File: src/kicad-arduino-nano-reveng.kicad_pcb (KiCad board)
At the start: 2 copper layers, 43.8 x 18.4 mm, 14 parts

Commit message: back layer components
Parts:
- removed the REF** at (111.8, 59.1)
- removed the REF** at (111.8, 57.6)
- removed the REF** at (111.8, 56.1)
- added REF**: Crystal_SMD_MicroCrystal_CC7V-T1A-2Pin_3.2x1.5mm, Crystal:Crystal_SMD_MicroCrystal_CC7V-T1A-2Pin_3.2x1.5mm, B.Cu at (85.6, 62.0)
- added REF**: C_0603_1608Metric, Capacitor_SMD:C_0603_1608Metric, B.Cu at (81.8, 61.5)
- added REF**: C_0603_1608Metric, Capacitor_SMD:C_0603_1608Metric, B.Cu at (91.4, 61.5)
- added REF**: C_0603_1608Metric, Capacitor_SMD:C_0603_1608Metric, B.Cu at (96.5, 55.9)
- added REF**: SOT-223, Package_TO_SOT_SMD:SOT-223, B.Cu at (110.7, 59.4)
- added REF**: SOIC-16_3.9x9.9mm_P1.27mm, Package_SO:SOIC-16_3.9x9.9mm_P1.27mm, B.Cu at (88.9, 56.8)
- added REF**: PinHeader_2x03_P2.54mm_Vertical, Connector_PinHeader_2.54mm:PinHeader_2x03_P2.54mm_Vertical, F.Cu at (117.3, 54.3)
- added REF**: C_0603_1608Metric, Capacitor_SMD:C_0603_1608Metric, B.Cu at (110.2, 52.3)
- added REF**: LED_0603_1608Metric_Pad1.05x0.95mm_HandSolder, LED_SMD:LED_0603_1608Metric_Pad1.05x0.95mm_HandSolder, F.Cu at (111.1, 59.3)
- added REF**: LED_0603_1608Metric_Pad1.05x0.95mm_HandSolder, LED_SMD:LED_0603_1608Metric_Pad1.05x0.95mm_HandSolder, F.Cu at (111.1, 57.7)
- added REF**: LED_0603_1608Metric_Pad1.05x0.95mm_HandSolder, LED_SMD:LED_0603_1608Metric_Pad1.05x0.95mm_HandSolder, F.Cu at (111.1, 56.0)
- added REF**: CP_EIA-3216-10_Kemet-I, Capacitor_Tantalum_SMD:CP_EIA-3216-10_Kemet-I, B.Cu at (110.2, 54.4)
- added REF**: CP_EIA-3216-10_Kemet-I, Capacitor_Tantalum_SMD:CP_EIA-3216-10_Kemet-I, B.Cu at (80.0, 52.8)
- added REF**: C_0603_1608Metric, Capacitor_SMD:C_0603_1608Metric, B.Cu at (79.2, 54.6)
- added REF**: D_SOD-123, Diode_SMD:D_SOD-123, B.Cu at (80.8, 56.8)
- added REF**: R_0603_1608Metric, Resistor_SMD:R_0603_1608Metric, B.Cu at (96.5, 57.9)
- added REF**: R_0603_1608Metric, Resistor_SMD:R_0603_1608Metric, B.Cu at (96.5, 59.4)
- added e: R_0603_1608Metric, Resistor_SMD:R_0603_1608Metric, B.Cu at (106.7, 62.5)
- REF** (x4): value R_0603_1608Metric_Pad1.05x0.95mm_HandSolder -> R_0603_1608Metric; footprint Resistor_SMD:R_0603_1608Metric_Pad1.05x0.95mm_HandSolder -> Resistor_SMD:R_0603_1608Metric
- REF**: value USB_Mini-B_Wuerth_65100516121_Horizontal -> USB_Mini-B_Lumberg_2486_01_Horizontal; footprint Connector_USB:USB_Mini-B_Wuerth_65100516121_Horizontal -> Connector_USB:USB_Mini-B_Lumberg_2486_01_Horizontal
- moved REF** 0.68 mm to (111.1, 54.4)
- moved REF** 0.68 mm to (108.0, 59.3)
- moved REF** 0.68 mm to (108.0, 54.4)
- moved REF** 0.64 mm to (108.0, 56.0)
- moved REF** 0.64 mm to (108.0, 57.7)
- moved REF** 0.64 mm to (81.3, 56.8)
- moved REF** 0.63 mm to (99.7, 52.1)
- moved REF** 0.31 mm to (117.2, 48.9)
- moved REF** 0.31 mm to (117.2, 64.8)

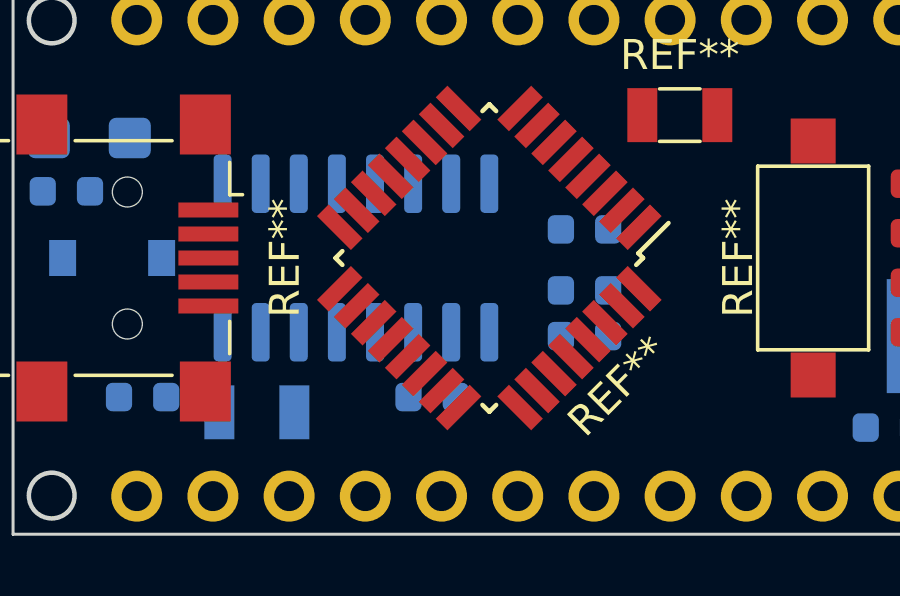
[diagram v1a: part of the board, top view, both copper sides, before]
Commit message: Sch front side components
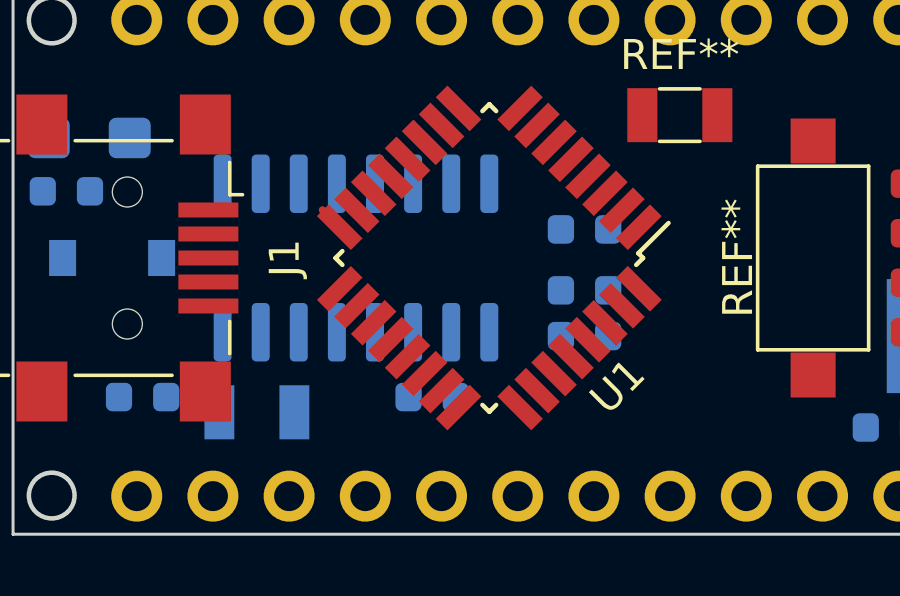
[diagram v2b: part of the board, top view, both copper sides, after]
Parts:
- renumbered REF** to J1, REF** to U1
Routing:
- net (no net): track 0.00 -> 1.71 mm

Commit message: Wiring
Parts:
- removed REF** (x3): LED_0603_1608Metric_Pad1.05x0.95mm_HandSolder, LED_SMD:LED_0603_1608Metric_Pad1.05x0.95mm_HandSolder
- added D2: TX, LED_SMD:LED_0603_1608Metric_Pad1.05x0.95mm_HandSolder, F.Cu at (111.1, 56.0)
- added D3: PWR, LED_SMD:LED_0603_1608Metric_Pad1.05x0.95mm_HandSolder, F.Cu at (111.1, 57.7)
- added D4: L, LED_SMD:LED_0603_1608Metric_Pad1.05x0.95mm_HandSolder, F.Cu at (111.1, 59.3)
- C1, C6: renamed from REF**; value CP_EIA-3216-10_Kemet-I -> CP
- C2, C3, C4, C5, C7: renamed from REF**; value C_0603_1608Metric -> C
- D1: renamed from REF**; value LED_0603_1608Metric_Pad1.05x0.95mm_HandSolder -> RX
- D5: renamed from REF**; value D_SOD-123 -> D_Schottky
- J1: value USB_Mini-B_Lumberg_2486_01_Horizontal -> USB_B_Mini
- J2: renamed from REF**; value PinHeader_2x03_P2.54mm_Vertical -> ISP
- J3, J4: renamed from REF**; value PinHeader_1x15_P2.54mm_Vertical -> Conn_01x15
- R1: renamed from e; value R_0603_1608Metric -> 103
- R2, R3: renamed from REF**; value R_0603_1608Metric -> R
- R4, R5, R6, R7: renamed from REF**; value R_0603_1608Metric -> 102
- SW1: renamed from REF**; value SW_SPST_CK_RS282G05A3 -> RESET
- U1: renamed from REF**; value SOT-223 -> AMS1117-5.0
- U2: renamed from U1; value TQFP-32_7x7mm_P0.8mm -> ATmega328P-AU
- U3: renamed from REF**; value SOIC-16_3.9x9.9mm_P1.27mm -> CH340G
- Y1: renamed from REF**; value Crystal_SMD_3215-2Pin_3.2x1.5mm -> Crystal_Atmega
- Y2: renamed from REF**; value Crystal_SMD_MicroCrystal_CC7V-T1A-2Pin_3.2x1.5mm -> Crystal
- moved J2 5.65 mm to (119.9, 59.4), turned to 180 degrees
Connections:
- C1 pad 1: (no net) -> +5V
- C1 pad 2: (no net) -> GND
- C2 pad 1: (no net) -> +5V
- C2 pad 2: (no net) -> GND
- C3 pad 1: (no net) -> RST
- C3 pad 2: (no net) -> DTR
- C4 pad 1: (no net) -> GND
- C4 pad 2: (no net) -> AREF
- C5 pad 1: (no net) -> GND
- C5 pad 2: (no net) -> 3V3
- C6 pad 1: (no net) -> VUSB
- C6 pad 2: (no net) -> GND
- C7 pad 1: (no net) -> VUSB
- C7 pad 2: (no net) -> GND
- D1 pad 1: (no net) -> RX0
- D1 pad 2: (no net) -> Net-(D1-Pad2)
- D5 pad 1: (no net) -> +5V
- D5 pad 2: (no net) -> VUSB
- J1 pad 1: (no net) -> VUSB
- J1 pad 2: (no net) -> D-
- J1 pad 3: (no net) -> D+
- J1 pad 4: (no net) -> Net-(J1-Pad4)
- J1 pad 5: (no net) -> GND
- J1 pad 6: (no net) -> GND
- J2 pad 1: (no net) -> D12
- J2 pad 2: (no net) -> +5V
- J2 pad 3: (no net) -> D13
- J2 pad 4: (no net) -> D11
- J2 pad 5: (no net) -> RST
- J2 pad 6: (no net) -> GND
- J3 pad 1: (no net) -> TX1
- J3 pad 10: (no net) -> D7
- J3 pad 11: (no net) -> D8
- J3 pad 12: (no net) -> D9
- J3 pad 13: (no net) -> D10
- J3 pad 14: (no net) -> D11
- J3 pad 15: (no net) -> D12
- J3 pad 2: (no net) -> RX0
- J3 pad 3: (no net) -> RST
- J3 pad 4: (no net) -> GND
- J3 pad 5: (no net) -> D2
- J3 pad 6: (no net) -> D3
- J3 pad 7: (no net) -> D4
- J3 pad 8: (no net) -> D5
- J3 pad 9: (no net) -> D6
- J4 pad 1: (no net) -> VIN
- J4 pad 10: (no net) -> A2
- J4 pad 11: (no net) -> A1
- J4 pad 12: (no net) -> A0
- J4 pad 13: (no net) -> AREF
- J4 pad 14: (no net) -> 3V3
- J4 pad 15: (no net) -> D13
- J4 pad 2: (no net) -> GND
- J4 pad 3: (no net) -> RST
- J4 pad 4: (no net) -> +5V
- J4 pad 5: (no net) -> A7
- J4 pad 6: (no net) -> A6
- J4 pad 7: (no net) -> A5
- J4 pad 8: (no net) -> A4
- J4 pad 9: (no net) -> A3
- R1 pad 1: (no net) -> +5V
- R1 pad 2: (no net) -> RST
- R2 pad 1: (no net) -> RXD
- R2 pad 2: (no net) -> TX1
- R3 pad 1: (no net) -> TXD
- R3 pad 2: (no net) -> RX0
- R4 pad 1: (no net) -> Net-(D1-Pad2)
- R4 pad 2: (no net) -> +5V
- R5 pad 1: (no net) -> Net-(D2-Pad2)
- R5 pad 2: (no net) -> +5V
- R6 pad 1: (no net) -> Net-(D3-Pad2)
- R6 pad 2: (no net) -> +5V
- R7 pad 1: (no net) -> Net-(D4-Pad2)
- R7 pad 2: (no net) -> D13
- SW1 pad 1: (no net) -> RST
- SW1 pad 2: (no net) -> GND
- U1 pad 1: (no net) -> GND
- U1 pad 2: (no net) -> +5V
- U1 pad 3: (no net) -> VIN
- U2 pad 1: (no net) -> D3
- U2 pad 10: (no net) -> D6
- U2 pad 11: (no net) -> D7
- U2 pad 12: (no net) -> D8
- U2 pad 13: (no net) -> D9
- U2 pad 14: (no net) -> D10
- U2 pad 15: (no net) -> D11
- U2 pad 16: (no net) -> D12
- U2 pad 17: (no net) -> D13
- U2 pad 18: (no net) -> +5V
- U2 pad 19: (no net) -> A6
- U2 pad 2: (no net) -> D4
- U2 pad 20: (no net) -> AREF
- U2 pad 21: (no net) -> GND
- U2 pad 22: (no net) -> A7
- U2 pad 23: (no net) -> A0
- U2 pad 24: (no net) -> A1
- U2 pad 25: (no net) -> A2
- U2 pad 26: (no net) -> A3
- U2 pad 27: (no net) -> A4
- U2 pad 28: (no net) -> A5
- U2 pad 29: (no net) -> RST
- U2 pad 3: (no net) -> GND
- U2 pad 30: (no net) -> RX0
- U2 pad 31: (no net) -> TX1
- U2 pad 32: (no net) -> D2
- U2 pad 4: (no net) -> +5V
- U2 pad 5: (no net) -> GND
- U2 pad 6: (no net) -> +5V
- U2 pad 7: (no net) -> XTAL1
- U2 pad 8: (no net) -> XTAL2
- U2 pad 9: (no net) -> D5
- U3 pad 1: (no net) -> GND
- U3 pad 10: (no net) -> Net-(U3-Pad10)
- U3 pad 11: (no net) -> Net-(U3-Pad11)
- U3 pad 12: (no net) -> Net-(U3-Pad12)
- U3 pad 13: (no net) -> DTR
- U3 pad 14: (no net) -> Net-(U3-Pad14)
- U3 pad 15: (no net) -> Net-(U3-Pad15)
- U3 pad 16: (no net) -> +5V
- U3 pad 2: (no net) -> TXD
- U3 pad 3: (no net) -> RXD
- U3 pad 4: (no net) -> 3V3
- U3 pad 5: (no net) -> D+
- U3 pad 6: (no net) -> D-
- U3 pad 7: (no net) -> XI
- U3 pad 8: (no net) -> XO
- U3 pad 9: (no net) -> Net-(U3-Pad9)
- Y1 pad 1: (no net) -> XTAL1
- Y1 pad 2: (no net) -> XTAL2
- Y2 pad 1: (no net) -> XO
- Y2 pad 2: (no net) -> XI
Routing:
- net (no net): track 1.71 -> 0.00 mm
- net GND: track 0.00 -> 0.87 mm
- net D12: track 0.00 -> 0.81 mm

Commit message: Almost finishing routing
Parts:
- U1: footprint Package_TO_SOT_SMD:SOT-223 -> Package_TO_SOT_SMD:SOT-223-3_TabPin2
- moved C2 0.51 mm to (110.2, 52.8)
- moved C1 0.51 mm to (110.2, 54.9)
- turned D2 to 180 degrees
- turned D3 to 180 degrees
- turned D4 to 180 degrees
- turned C3 to 180 degrees
- turned C4 to 180 degrees
- turned C7 to 180 degrees
- turned D1 to 180 degrees
- turned R1 to 180 degrees
- turned R4 to 180 degrees
- turned R5 to 180 degrees
- turned R6 to 180 degrees
- turned R7 to 180 degrees
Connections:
- U2 pad 5: GND -> (no net)
- U2 pad 6: +5V -> (no net)
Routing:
- net +5V: track 0.03 -> 69.3 mm, vias 0 -> 2
- net RST: track 0.00 -> 57.1 mm, vias 0 -> 2
- net D12: track 0.81 -> 54.9 mm
- net D13: track 0.00 -> 46.0 mm, vias 0 -> 2
- net D11: track 0.00 -> 45.1 mm
- net GND: track 0.87 -> 40.3 mm, vias 0 -> 7
- net TX1: track 0.00 -> 32.0 mm, vias 0 -> 1
- net RX0: track 0.00 -> 30.6 mm, vias 0 -> 2
- net D2: track 0.00 -> 14.1 mm
- net 3V3: track 0.00 -> 13.4 mm
- net VUSB: track 0.00 -> 10.9 mm, vias 0 -> 1
- net D3: track 0.00 -> 10.7 mm
- net D4: track 0.00 -> 9.38 mm
- net D5: track 0.00 -> 8.28 mm
- net A5: track 0.00 -> 8.03 mm
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- added copper zone on B.Cu, net GND
- added copper zone on F.Cu, net GND
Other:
- net class Power added: clearance 0.2, trace_width 0.3, via_dia 0.8, via_drill 0.4
- net class VIN added: clearance 0.2, trace_width 0.5, via_dia 0.8, via_drill 0.4
- board text added: "1"
- board text added: "2"

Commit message: Finished wiring
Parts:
- U1: footprint Package_TO_SOT_SMD:SOT-223-3_TabPin2 -> igorkelvin:SOT-223-3_TabPin2
- moved C5 1.78 mm to (80.0, 61.5)
- moved Y2 1.53 mm to (84.1, 61.8)
- moved C1 0.38 mm to (110.2, 54.5)
- moved R1 0.25 mm to (106.7, 62.2)
- moved C2 0.25 mm to (110.2, 52.6)
- moved U1 0.25 mm to (110.7, 59.2)
- moved C6 0.13 mm to (80.0, 52.7)
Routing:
- net A6: track 0.00 -> 22.4 mm, vias 0 -> 1
- net A7: track 0.00 -> 18.5 mm
- net AREF: track 7.30 -> 14.4 mm
- net 3V3: track 13.4 -> 15.4 mm
- net GND: track 40.3 -> 39.3 mm, vias 7 -> 8
- net XO: track 2.71 -> 3.34 mm

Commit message: PCB Rev0
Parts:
- moved Y1 110.0 mm to (208.4, 68.8)
- moved C1 110.0 mm to (218.9, 71.2)
- moved C2 110.0 mm to (218.9, 69.3)
- moved C3 110.0 mm to (205.2, 72.6)
- moved C5 110.0 mm to (188.7, 78.2)
- moved C6 110.0 mm to (188.7, 69.5)
- moved C7 110.0 mm to (188.0, 71.4)
- moved D2 110.0 mm to (219.8, 72.8)
- moved D5 110.0 mm to (189.5, 73.6)
- moved R2 110.0 mm to (205.2, 74.7)
- moved R3 110.0 mm to (205.2, 76.2)
- moved R4 110.0 mm to (216.7, 71.1)
- moved R5 110.0 mm to (216.7, 72.8)
- moved R6 110.0 mm to (216.7, 74.4)
- moved R7 110.0 mm to (216.7, 76.1)
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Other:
- board text added: "+5V"
- board text added: "3V3"
- board text added: "A0"
- board text added: "A1"
- board text added: "A2"
- board text added: "A3"
- board text added: "A4"
- board text added: "A5"
- board text added: "A6"
- board text added: "A7"
- board text added: "AREF"
- board text added: "D10"
- board text added: "D11"
- board text added: "D12"
- board text added: "D13"
- board text added: "D2"
- board text added: "D3"
- board text added: "D4"
- board text added: "D5"
- board text added: "D6"
- board text added: "D7"
- board text added: "D8"
- board text added: "D9"
- board text added: "GND"
- board text added: "RST"
- board text added: "RX0"
- board text added: "TX1"
- board text added: "VIN"
- board text removed: "2"
